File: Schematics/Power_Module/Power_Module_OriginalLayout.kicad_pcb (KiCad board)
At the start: 4 copper layers, 69.5 x 60 mm, 110 parts, among them J1 ScrewSwitch A, J2 ScrewSwitch B, J3 Battery B, J4 USB_C_Female_USB2_Small, J5 Battery A, J6 Stack Male Edge Connector, Q1 AO4447A, Q2 AO4447A, U1 LMR51430XDDCR, U10 ISO1042BDWVR, U11 LM66100DCKR, U12 LM66100DCKR, U13 LM66100DCKR, U14 LM66100DCKR, U15 LM66100DCKR, U2 LMR51430XDDCR, U3 LMR51430XDDCR, U4 STM32F103C8Tx, U5 STM32F103C8Tx, U6 ACS37041KLHBLT-010B3, U7 ACS37041KLHBLT-010B3, U8 ACS37041KLHBLT-010B3, U9 AMS1117-3.3, Y1 X322516MMB4SI

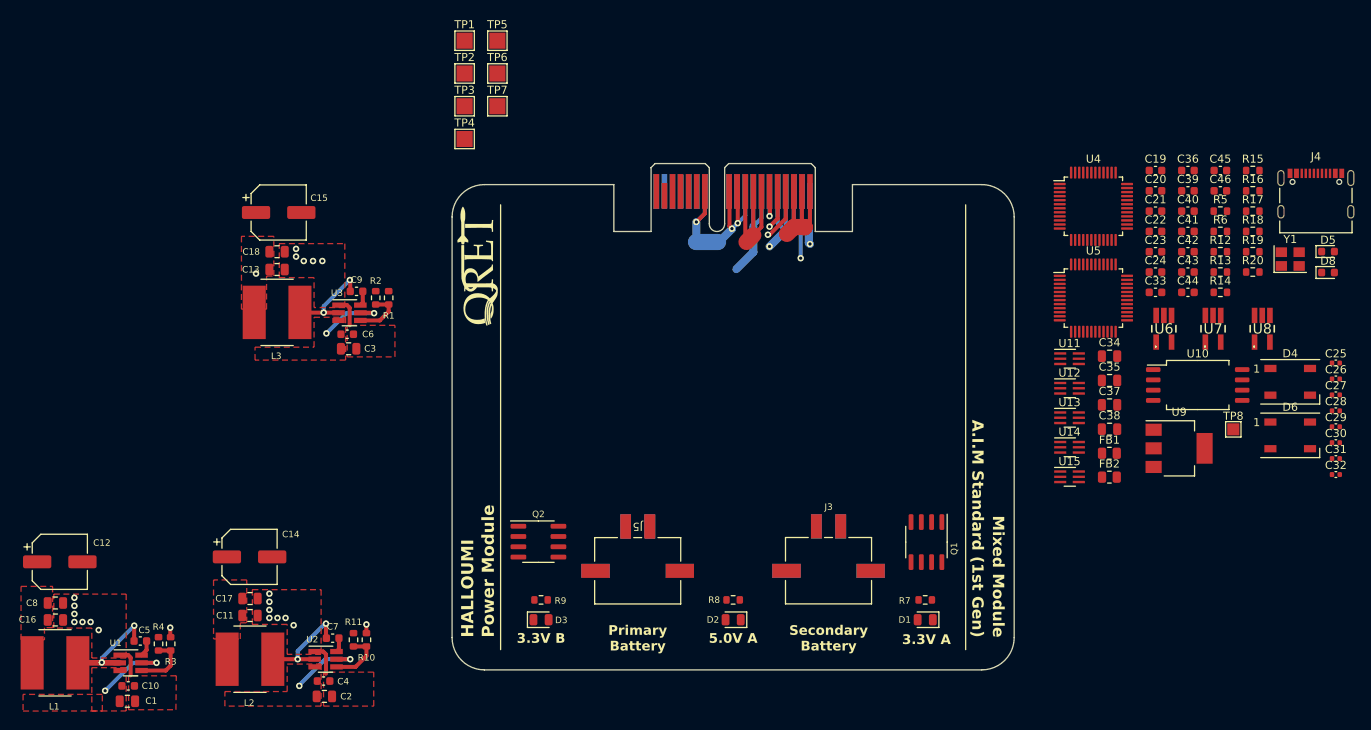
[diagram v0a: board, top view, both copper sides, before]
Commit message: Added MCUs + sensors to schematic
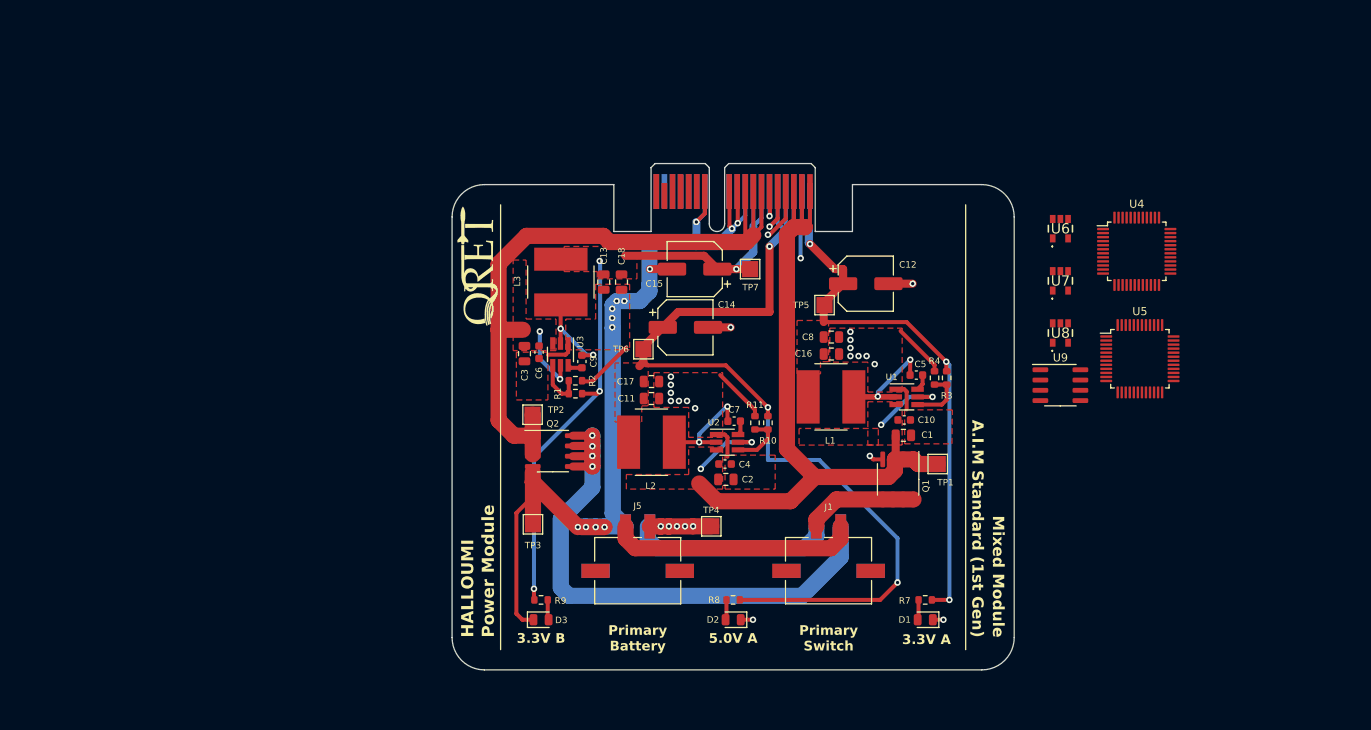
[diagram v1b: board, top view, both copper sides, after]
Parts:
- removed C19, C20: 10uF, Capacitor_SMD:C_0603_1608Metric
- removed C21, C22, C44, C45, C46: 0.1u, Capacitor_SMD:C_0603_1608Metric
- removed C23, C24: 10p, Capacitor_SMD:C_0603_1608Metric
- removed C25, C26, C27, C28, C29, C30, C31, C32: 100n, Capacitor_SMD:C_0402_1005Metric
- removed C33, C36: 10n, Capacitor_SMD:C_0603_1608Metric
- removed C34, C35, C37, C38: 1uF, Capacitor_SMD:C_0805_2012Metric
- removed C39, C40, C41, C42, C43: 1uF, Capacitor_SMD:C_0603_1608Metric
- removed D4, D6: WS2812B, LED_SMD:LED_WS2812B_PLCC4_5.0x5.0mm_P3.2mm
- removed D5, D8: DB_LED (YLW), LED_SMD:LED_0603_1608Metric
- removed FB1, FB2: 100R, Resistor_SMD:R_0805_2012Metric
- removed J4: USB_C_Female_USB2_Small, footprints:USB_C_DB-108PWB
- removed R12, R15, R5: 30k, Resistor_SMD:R_0603_1608Metric
- removed R13, R6: 10k, Resistor_SMD:R_0603_1608Metric
- removed R14: 60k, Resistor_SMD:R_0603_1608Metric
- removed R16: 1.5k, Resistor_SMD:R_0603_1608Metric
- removed R17, R18: 5.1k, Resistor_SMD:R_0603_1608Metric
- removed R19, R20: 680R, Resistor_SMD:R_0603_1608Metric
- removed TP8: TP_GND, TestPoint:TestPoint_Pad_1.5x1.5mm
- removed U10: ISO1042BDWVR, ISO1042:SOIC-8 ISO1042BDWV
- removed U11, U12, U13, U14, U15: LM66100DCKR, LMR66100:SC-70-6_Handsoldering
- removed Y1: X322516MMB4SI, Crystal:Crystal_SMD_3225-4Pin_3.2x2.5mm
- J1: renamed from J3; value Battery B -> ScrewSwitch A
- J3: renamed from J1; value ScrewSwitch A -> Battery B
- R7: value 3.3k -> 1.2k
- U6, U7, U8: footprint footprints:APS12628LLHALTBAP_HandSolder -> footprints:APS12628LLHALTBAP
- U9: value AMS1117-3.3 -> ISO6421 OR SMTHN; footprint Package_TO_SOT_SMD:SOT-223-3_TabPin2 -> Package_SO:SOIC-8_3.9x4.9mm_P1.27mm
- moved C12 105.4 mm to (181.4, 52.0)
- moved C1 101.4 mm to (186.1, 70.8)
- moved C10 101.4 mm to (186.2, 68.8)
- moved C16 101.4 mm to (177.2, 60.7)
- moved C5 101.4 mm to (187.7, 63.3)
- moved C8 101.4 mm to (177.2, 58.6)
- moved R3 101.4 mm to (191.4, 63.6)
- moved R4 101.4 mm to (189.9, 63.6)
- moved L1 101.4 mm to (177.1, 66.0)
- moved U1 101.4 mm to (186.4, 66.0)
- moved TP1 78.5 mm to (190.3, 74.3)
- moved C14 60.9 mm to (159.1, 57.4)
- moved TP4 56.8 mm to (162.3, 82.0)
- moved R10 56.4 mm to (169.3, 69.2)
- moved C17 56.4 mm to (154.9, 64.1)
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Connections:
- C11 pad 1: 5.0V_A_Pre -> 5.0V_A
- C12 pad 1: 3.3V_A_Pre -> 3.3V_A
- C13 pad 1: 3.3V_B_Pre -> 3.3V_B
- C14 pad 1: 5.0V_A_Pre -> 5.0V_A
- C15 pad 1: 3.3V_B_Pre -> 3.3V_B
- C16 pad 1: 3.3V_A_Pre -> 3.3V_A
- C17 pad 1: 5.0V_A_Pre -> 5.0V_A
- C18 pad 1: 3.3V_B_Pre -> 3.3V_B
- C8 pad 1: 3.3V_A_Pre -> 3.3V_A
- J1 pad 1: GND2 -> Net-(J1-Pad1)
- J1 pad 2: Net-(J2-Pad1) -> Net-(J1-Pad2)
- J3 pad 1: Net-(J1-Pad1) -> GND2
- J3 pad 2: Net-(J1-Pad2) -> Net-(J2-Pad1)
- J6 pad B13: CAN_L -> unconnected-(J6-CAN_L-PadB13)
- J6 pad B14: CAN_H -> unconnected-(J6-CAN_H-PadB14)
- L1 pad 2: 3.3V_A_Pre -> 3.3V_A
- L2 pad 2: 5.0V_A_Pre -> 5.0V_A
- L3 pad 2: 3.3V_B_Pre -> 3.3V_B
- R1 pad 1: 3.3V_B_Pre -> 3.3V_B
- R10 pad 1: 5.0V_A_Pre -> 5.0V_A
- R3 pad 1: 3.3V_A_Pre -> 3.3V_A
- TP5 pad 1: 3.3V_A_Pre -> 3.3V_A
- TP6 pad 1: 5.0V_A_Pre -> 5.0V_A
- TP7 pad 1: 3.3V_B_Pre -> 3.3V_B
- U4 pad 1: Net-(U4-VBAT) -> unconnected-(U4-VBAT-Pad1)
- U4 pad 20: BOOT1_A -> unconnected-(U4-PB2-Pad20)
- U4 pad 23: GND -> Net-(U4-VSS-Pad23)
- U4 pad 24: Net-(U4-VBAT) -> unconnected-(U4-VDD-Pad24)
- U4 pad 34: SWDIO_A -> unconnected-(U4-PA13-Pad34)
- U4 pad 35: GND -> Net-(U4-VSS-Pad23)
- U4 pad 36: Net-(U4-VBAT) -> unconnected-(U4-VDD-Pad36)
- U4 pad 37: SWCLK_A -> unconnected-(U4-PA14-Pad37)
- U4 pad 38: DB_LED_A -> unconnected-(U4-PA15-Pad38)
- U4 pad 39: RGB_DATA -> unconnected-(U4-PB3-Pad39)
- U4 pad 44: BOOT0_A -> unconnected-(U4-BOOT0-Pad44)
- U4 pad 45: CAN_RX -> unconnected-(U4-PB8-Pad45)
- U4 pad 46: CAN_TX -> unconnected-(U4-PB9-Pad46)
- U4 pad 47: GND -> Net-(U4-VSS-Pad23)
- U4 pad 48: Net-(U4-VBAT) -> unconnected-(U4-VDD-Pad48)
- U4 pad 7: STM_RESET_A -> unconnected-(U4-NRST-Pad7)
- U4 pad 8: GND -> unconnected-(U4-VSSA-Pad8)
- U5 pad 20: BOOT1_B -> unconnected-(U5-PB2-Pad20)
- U5 pad 23: GND2 -> Net-(U5-VSS-Pad23)
- U5 pad 32: USB_D- -> unconnected-(U5-PA11-Pad32)
- U5 pad 33: USB_D+ -> unconnected-(U5-PA12-Pad33)
- U5 pad 34: SWDIO_B -> unconnected-(U5-PA13-Pad34)
- U5 pad 35: GND2 -> Net-(U5-VSS-Pad23)
- U5 pad 37: SWCLK_B -> unconnected-(U5-PA14-Pad37)
- U5 pad 38: DB_LED_B -> unconnected-(U5-PA15-Pad38)
- U5 pad 44: BOOT0_B -> unconnected-(U5-BOOT0-Pad44)
- U5 pad 47: GND2 -> Net-(U5-VSS-Pad23)
- U5 pad 5: OSC_IN -> unconnected-(U5-PD0-Pad5)
- U5 pad 6: OSC_OUT -> unconnected-(U5-PD1-Pad6)
- U5 pad 7: STM_RESET_B -> unconnected-(U5-NRST-Pad7)
- U5 pad 8: GND2 -> unconnected-(U5-VSSA-Pad8)
- U6 pad 1: 3.3V_A_Pre -> unconnected-(U6-IP+-Pad1)
- U6 pad 2: 3.3V_A -> unconnected-(U6-IP--Pad2)
- U6 pad 3: GND -> unconnected-(U6-GND-Pad3)
- U6 pad 5: V_MUX_A -> unconnected-(U6-VDD-Pad5)
- U7 pad 1: 5.0V_A_Pre -> unconnected-(U7-IP+-Pad1)
- U7 pad 2: 5.0V_A -> unconnected-(U7-IP--Pad2)
- U7 pad 3: GND -> unconnected-(U7-GND-Pad3)
- U7 pad 5: V_MUX_A -> unconnected-(U7-VDD-Pad5)
- U8 pad 1: 3.3V_B_Pre -> unconnected-(U8-IP+-Pad1)
- U8 pad 2: 3.3V_B -> unconnected-(U8-IP--Pad2)
- U8 pad 3: GND2 -> unconnected-(U8-GND-Pad3)
- U8 pad 5: V_MUX_B -> unconnected-(U8-VDD-Pad5)
- U9 pad 1: GND2 -> unconnected-(U9-IP+_1-Pad1)
- U9 pad 2: V_REGUSB_B -> unconnected-(U9-IP+_2-Pad2)
- U9 pad 3: Net-(U9-VI) -> unconnected-(U9-IP-_1-Pad3)
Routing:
- net 5.0V_A: track 12.9 -> 111.7 mm, vias 1 -> 3
- net GND2: track 33.8 -> 129.0 mm, vias 8 -> 13
- net Net-(J2-Pad2): track 0.00 -> 74.8 mm, vias 0 -> 4
- net BATT_A: track 35.1 -> 103.2 mm
- net BATT_B: track 27.5 -> 92.1 mm
- net 3.3V_B: track 14.8 -> 78.5 mm, vias 1 -> 4
- net 3.3V_A: track 11.2 -> 74.2 mm, vias 1 -> 3
- net GND: track 33.7 -> 65.2 mm, vias 18 -> 28
- net Net-(J1-Pad1): track 0.00 -> 30.6 mm
- net Net-(J2-Pad1): track 0.00 -> 24.7 mm
- net Net-(J1-Pad2): track 0.00 -> 13.9 mm
- net Net-(D3-A): track 0.00 -> 2.50 mm
- net Net-(D2-A): track 0.00 -> 2.50 mm
- net Net-(D1-A): track 0.00 -> 2.50 mm
- net 3.3V_A_Pre: track 1.20 -> 0.00 mm, vias 1 -> 0
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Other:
- board text added: "Halloumi Rev 2.0 QRET Feb 2025 Rajan Laird Kennan Bays Oak Campbell"
- board text removed: "locked"
